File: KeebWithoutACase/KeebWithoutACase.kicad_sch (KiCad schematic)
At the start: 0 parts

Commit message: completed the first row of switches and diodes
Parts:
- added D1, D10, D11, D12, D13, D14, D2, D3, D4, D5, D6, D7, D8, D9: 1N4148WT, Diode_SMD:D_SOD-523, symbol Diode:1N4148WT
- added SW1, SW10, SW11, SW12, SW13, SW14, SW2, SW3, SW4, SW5, SW6, SW7, SW8, SW9: SW_Push_45deg, symbol Switch:SW_Push_45deg
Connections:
- new net: D13.2 (A), SW13.2
- new net: D9.2 (A), SW9.2
- new net: D7.2 (A), SW7.2
- new net: D6.2 (A), SW6.2
- new net: D14.2 (A), SW14.2
- new net: D3.2 (A), SW3.2
- new net: D11.2 (A), SW11.2
- new net: D12.2 (A), SW12.2
- new net: D2.2 (A), SW2.2
- new net: D1.2 (A), SW1.2
- new net: D10.2 (A), SW10.2
- new net: D8.2 (A), SW8.2
- new net: D5.2 (A), SW5.2
- new net: D4.2 (A), SW4.2

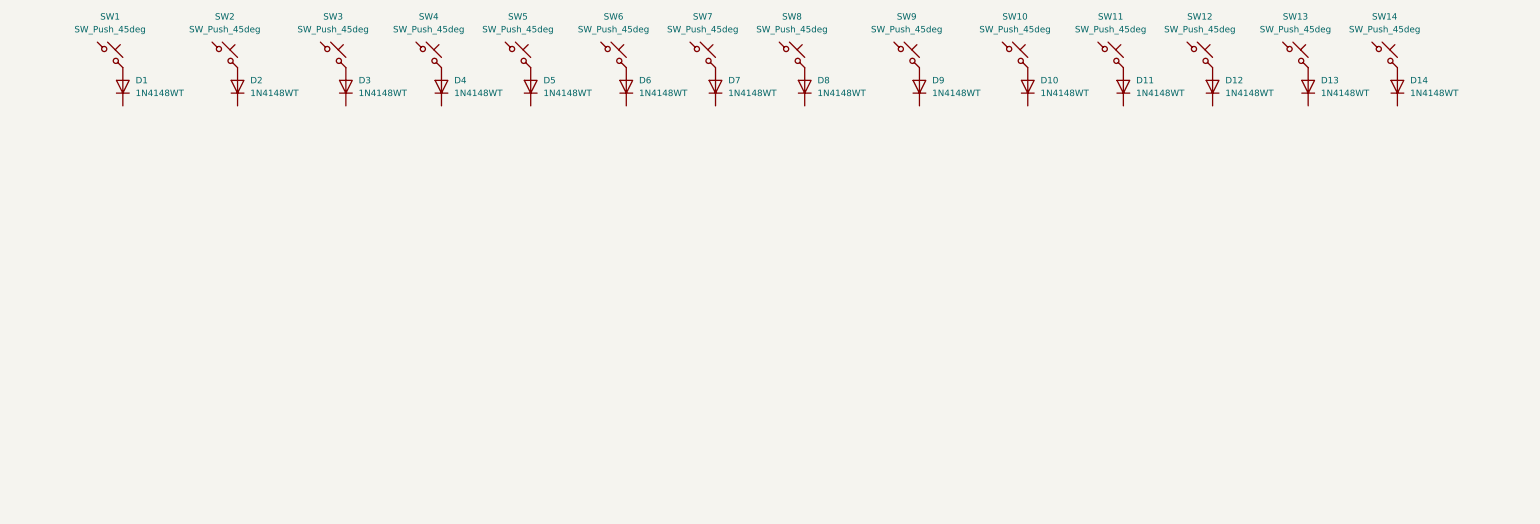
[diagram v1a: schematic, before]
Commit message: layed out the switches and diodes for the 2nd and third row
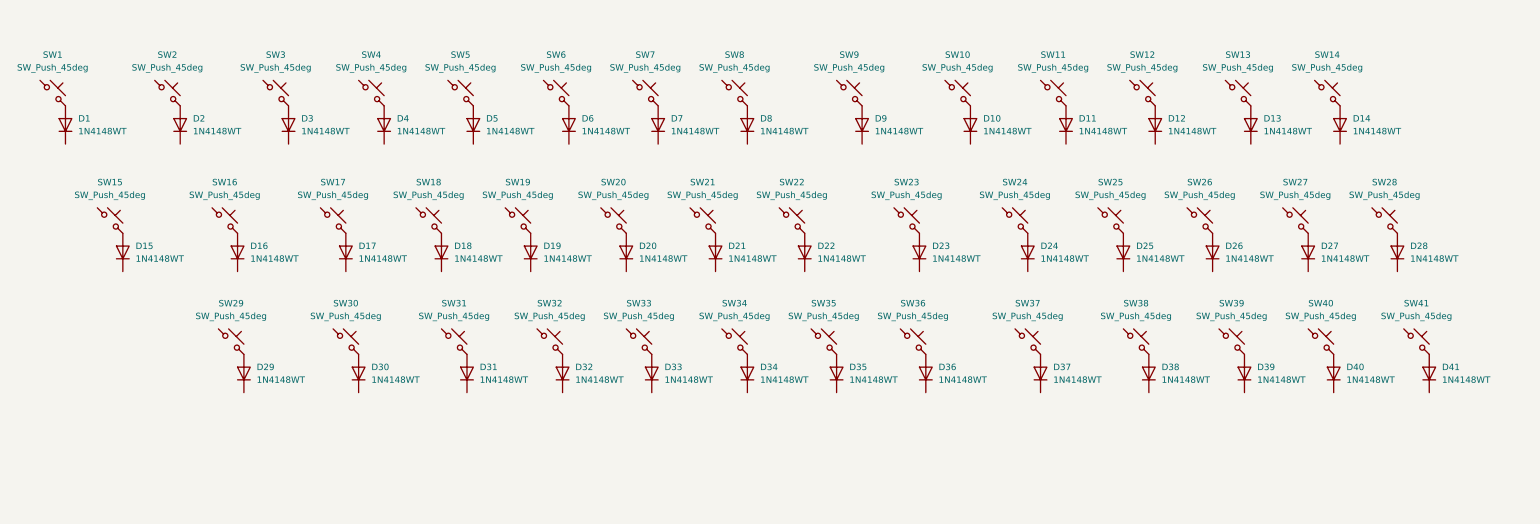
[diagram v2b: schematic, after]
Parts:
- added D15, D16, D17, D18, D19, D20, D21, D22, D23, D24, D25, D26, D27, D28, D29, D30, D31, D32, D33, D34, D35, D36, D37, D38, D39, D40, D41: 1N4148WT, Diode_SMD:D_SOD-523, symbol Diode:1N4148WT
- added SW15, SW16, SW17, SW18, SW19, SW20, SW21, SW22, SW23, SW24, SW25, SW26, SW27, SW28, SW29, SW30, SW31, SW32, SW33, SW34, SW35, SW36, SW37, SW38, SW39, SW40, SW41: SW_Push_45deg, symbol Switch:SW_Push_45deg
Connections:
- new net: D15.2 (A), SW15.2
- new net: D16.2 (A), SW16.2
- new net: D27.2 (A), SW27.2
- new net: D26.2 (A), SW26.2
- new net: D23.2 (A), SW23.2
- new net: D33.2 (A), SW33.2
- new net: D37.2 (A), SW37.2
- new net: D21.2 (A), SW21.2
- new net: D39.2 (A), SW39.2
- new net: D36.2 (A), SW36.2
- new net: D17.2 (A), SW17.2
- new net: D35.2 (A), SW35.2
- new net: D38.2 (A), SW38.2
- new net: D28.2 (A), SW28.2
- new net: D31.2 (A), SW31.2
- new net: D20.2 (A), SW20.2
- new net: D29.2 (A), SW29.2
- new net: D40.2 (A), SW40.2
- new net: D18.2 (A), SW18.2
- new net: D34.2 (A), SW34.2
- new net: D32.2 (A), SW32.2
- new net: D19.2 (A), SW19.2
- new net: D25.2 (A), SW25.2
- new net: D24.2 (A), SW24.2
- new net: D41.2 (A), SW41.2
- new net: D22.2 (A), SW22.2
- new net: D30.2 (A), SW30.2
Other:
- moved on the sheet: D1, D10, D11, D12, D13, D14, D2, D3, D4, D5, D6, D7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

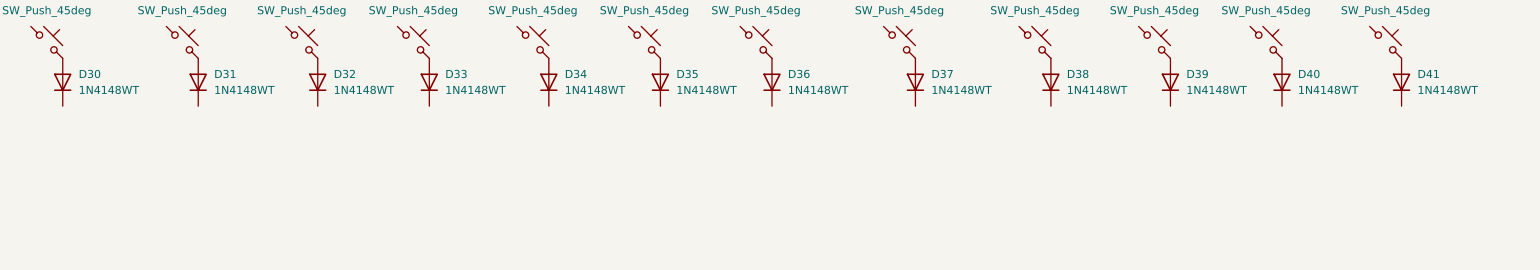
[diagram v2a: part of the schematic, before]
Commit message: added the switches and diodes for the final layer
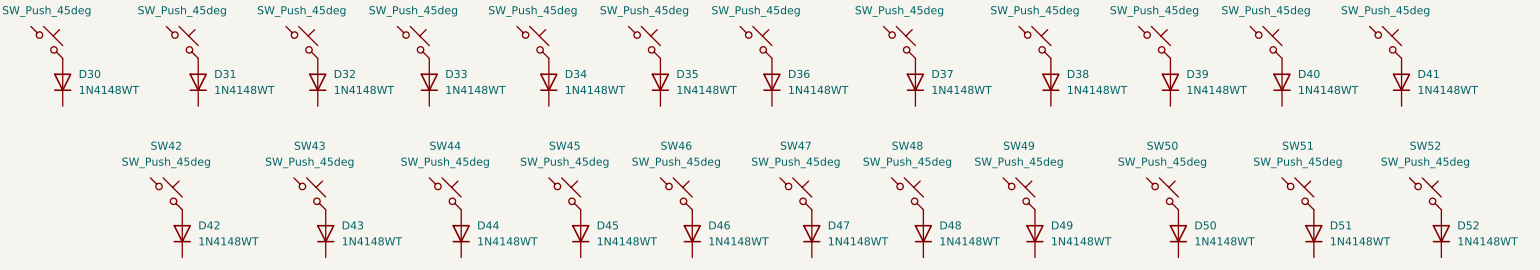
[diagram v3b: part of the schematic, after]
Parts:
- added D42, D43, D44, D45, D46, D47, D48, D49, D50, D51, D52: 1N4148WT, Diode_SMD:D_SOD-523, symbol Diode:1N4148WT
- added SW42, SW43, SW44, SW45, SW46, SW47, SW48, SW49, SW50, SW51, SW52: SW_Push_45deg, symbol Switch:SW_Push_45deg
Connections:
- new net: D51.2 (A), SW51.2
- new net: D44.2 (A), SW44.2
- new net: D50.2 (A), SW50.2
- new net: D49.2 (A), SW49.2
- new net: D52.2 (A), SW52.2
- new net: D48.2 (A), SW48.2
- new net: D45.2 (A), SW45.2
- new net: D42.2 (A), SW42.2
- new net: D43.2 (A), SW43.2
- new net: D47.2 (A), SW47.2
- new net: D46.2 (A), SW46.2
